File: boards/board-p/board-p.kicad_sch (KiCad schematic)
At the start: 25 parts, among them J1 TYPE-C-31-M-17, J2 PogoPad_1x4_NVM_I2C, J3 PogoPad_1x8_Debug, Q1 AO3401A, U1 STUSB4500QTR

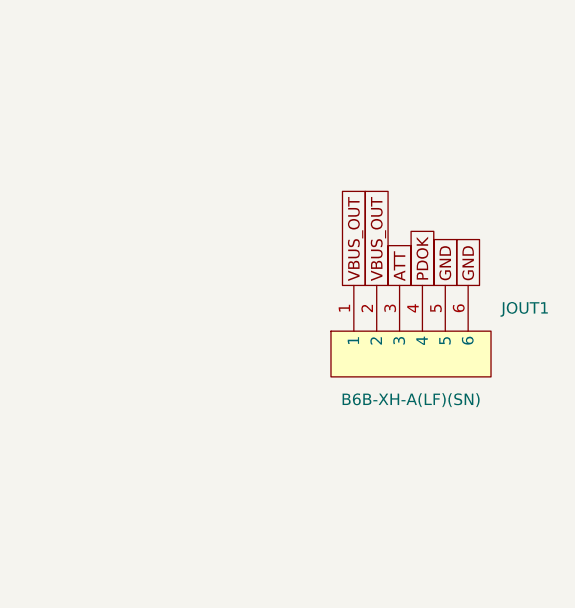
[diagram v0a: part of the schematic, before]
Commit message: feat(connectors): use XFCN board header pair
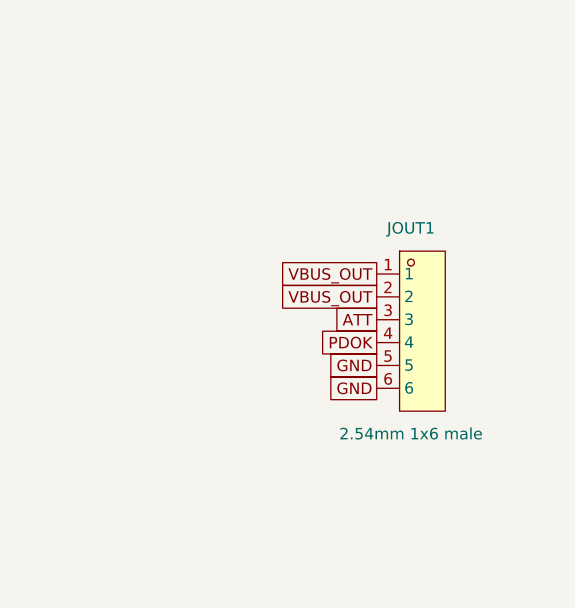
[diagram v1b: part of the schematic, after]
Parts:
- JOUT1: value B6B-XH-A(LF)(SN) -> 2.54mm 1x6 male; footprint zudo-led-lamp:CONN-TH_6P-P2.50_B6B-XH-A-LF-SN -> zudo-led-lamp:HDR-TH_6P-P2.54-V-M; symbol zudo-led-lamp:B6B-XH-A -> zudo-led-lamp:PZ254V-11-06P; LCSC C144397 -> C492405
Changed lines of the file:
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@@
 	)
 	(symbol
-		(lib_id "zudo-led-lamp:B6B-XH-A")
+		(lib_id "zudo-led-lamp:PZ254V-11-06P")
 		(at 317.5 88.9 0)
 		(unit 1)
@@
 		(dnp no)
 		(property "Reference" "JOUT1"
-			(at 330.2 86.36 0)
-			(effects
-				(font (size 1.27 1.27))
-			)
-		)
-		(property "Value" "B6B-XH-A(LF)(SN)"
-			(at 317.5 96.52 0)
-			(effects
-				(font (size 1.27 1.27))
-			)
-		)
-		(property "Footprint" "zudo-led-lamp:CONN-TH_6P-P2.50_B6B-XH-A-LF-SN"
+			(at 317.5 77.47 0)
+			(effects
+				(font (size 1.27 1.27))
+			)
+		)
+		(property "Value" "2.54mm 1x6 male"
+			(at 317.5 100.33 0)
+			(effects
+				(font (size 1.27 1.27))
+			)
+		)
+		(property "Footprint" "zudo-led-lamp:HDR-TH_6P-P2.54-V-M"
 			(at 317.5 88.9 0)
 			(effects
@@
 			)
 		)
-		(property "LCSC" "C144397"
+		(property "LCSC" "C492405"
 			(at 317.5 96.52 0)
 			(effects
@@
 	(global_label "VBUS_OUT"
 		(shape passive)
-		(at 311.15 83.82 90)
-		(effects
-			(font (size 1.27 1.27))
-			(justify left)
+		(at 313.69 82.55 180)
+		(effects
+			(font (size 1.27 1.27))
+			(justify right)
 		)
 	)
 	(global_label "VBUS_OUT"
 		(shape passive)
-		(at 313.69 83.82 90)
-		(effects
-			(font (size 1.27 1.27))
-			(justify left)
+		(at 313.69 85.09 180)
+		(effects
+			(font (size 1.27 1.27))
+			(justify right)
 		)
 	)
@@
 	(global_label "ATT"
 		(shape passive)
-		(at 316.23 83.82 90)
-		(effects
-			(font (size 1.27 1.27))
-			(justify left)
+		(at 313.69 87.63 180)
+		(effects
+			(font (size 1.27 1.27))
+			(justify right)
 		)
 	)
@@
 	(global_label "PDOK"
 		(shape passive)
-		(at 318.77 83.82 90)
-		(effects
-			(font (size 1.27 1.27))
-			(justify left)
+		(at 313.69 90.17 180)
+		(effects
+			(font (size 1.27 1.27))
+			(justify right)
 		)
 	)
@@
 	(global_label "GND"
 		(shape passive)
-		(at 321.31 83.82 90)
-		(effects
-			(font (size 1.27 1.27))
-			(justify left)
-		)
-	)
-	(global_label "GND"
-		(shape passive)
-		(at 323.85 83.82 90)
-		(effects
-			(font (size 1.27 1.27))
-			(justify left)
-		)
-	)
+		(at 313.69 92.71 180)
+		(effects
+			(font (size 1.27 1.27))
+			(justify right)
+		)
+	)
+	(global_label "GND"
+		(shape passive)
+		(at 313.69 95.25 180)
+		(effects
+			(font (size 1.27 1.27))
+			(justify right)
+		)
+	)
